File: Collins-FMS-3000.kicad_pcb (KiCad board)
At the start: 2 copper layers, 145 x 160 mm, 138 parts, among them J1 USB_B_Mini, J2 AVR-ISP-6, J3 Conn_01x04, SW1 SW_Push_LED, SW10 SW_Push_LED, SW11 SW_Push_LED, SW12 SW_Push_LED, SW13 SW_Push_LED, SW14 SW_Push_LED, SW15 SW_Push_LED, SW16 SW_Push_LED, SW17 SW_Push_LED, SW18 SW_Push_LED, SW19 SW_Push_LED, SW2 SW_Push_LED, SW20 SW_Push_LED, SW21 SW_Push_LED, SW22 SW_Push_LED, SW23 SW_Push_LED, SW24 SW_Push_LED, SW25 SW_Push_LED, SW26 SW_Push_LED, SW27 SW_Push_LED, SW28 SW_Push_LED, SW29 SW_Push_LED, SW3 SW_Push_LED, SW30 SW_Push_LED, SW31 SW_Push_LED, SW32 SW_Push_LED, SW33 SW_Push_LED, SW34 SW_Push_LED, SW35 SW_Push_LED, SW36 SW_Push_LED, SW37 SW_Push_LED, SW38 SW_Push_LED, SW39 SW_Push_LED, SW4 SW_Push_LED, SW40 SW_Push_LED, SW41 SW_Push_LED, SW42 SW_Push_LED, SW43 SW_Push_LED, SW44 SW_Push_LED, SW45 SW_Push_LED, SW46 SW_Push_LED, SW47 SW_Push_LED, SW48 SW_Push_LED, SW49 SW_Push_LED, SW5 SW_Push_LED, SW50 SW_Push_LED, SW51 SW_Push_LED, SW52 SW_Push_LED, SW53 SW_Push_LED, SW54 SW_Push_LED, SW55 SW_Push_LED, SW56 SW_Push_LED, SW57 SW_Push_LED, SW58 SW_Push_LED, SW59 SW_Push_LED, SW6 SW_Push_LED, SW60 SW_Push_LED, SW61 SW_Push_LED, SW62 SW_Push_LED, SW63 SW_Push_LED, SW64 SW_Push_LED, SW65 SW_Push_LED, SW66 SW_Push_LED, SW67 SW_Push_LED, SW68 SW_Push_LED, SW69 SW_Push_LED, SW7 SW_Push_LED, SW70 SW_Push, SW8 SW_Push_LED, SW9 SW_Push_LED, U1 ATmega32U4-MU, U2 MCP23017_SO, U3 MCP23017_SO, U4 IS31FL3733B, Y1 16MHz

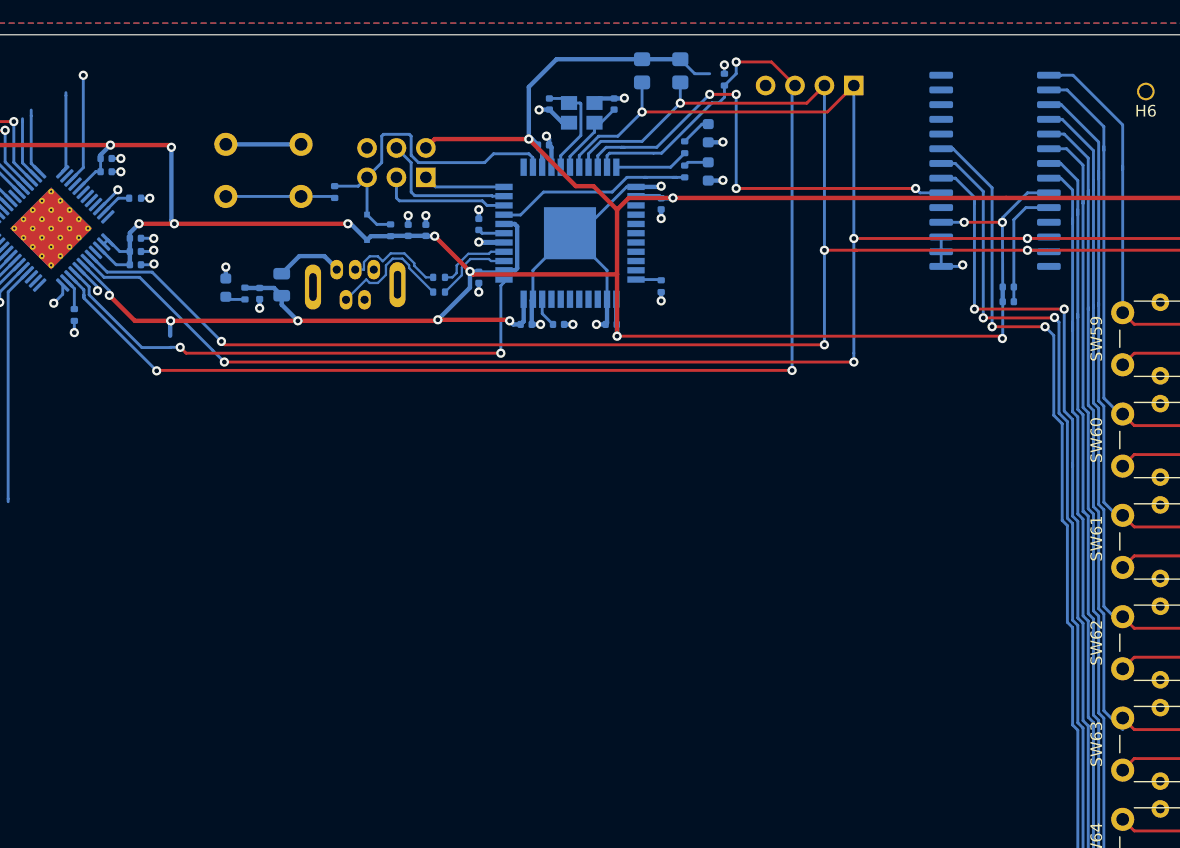
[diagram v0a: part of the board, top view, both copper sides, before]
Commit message: Add ROW INTB, new debug header
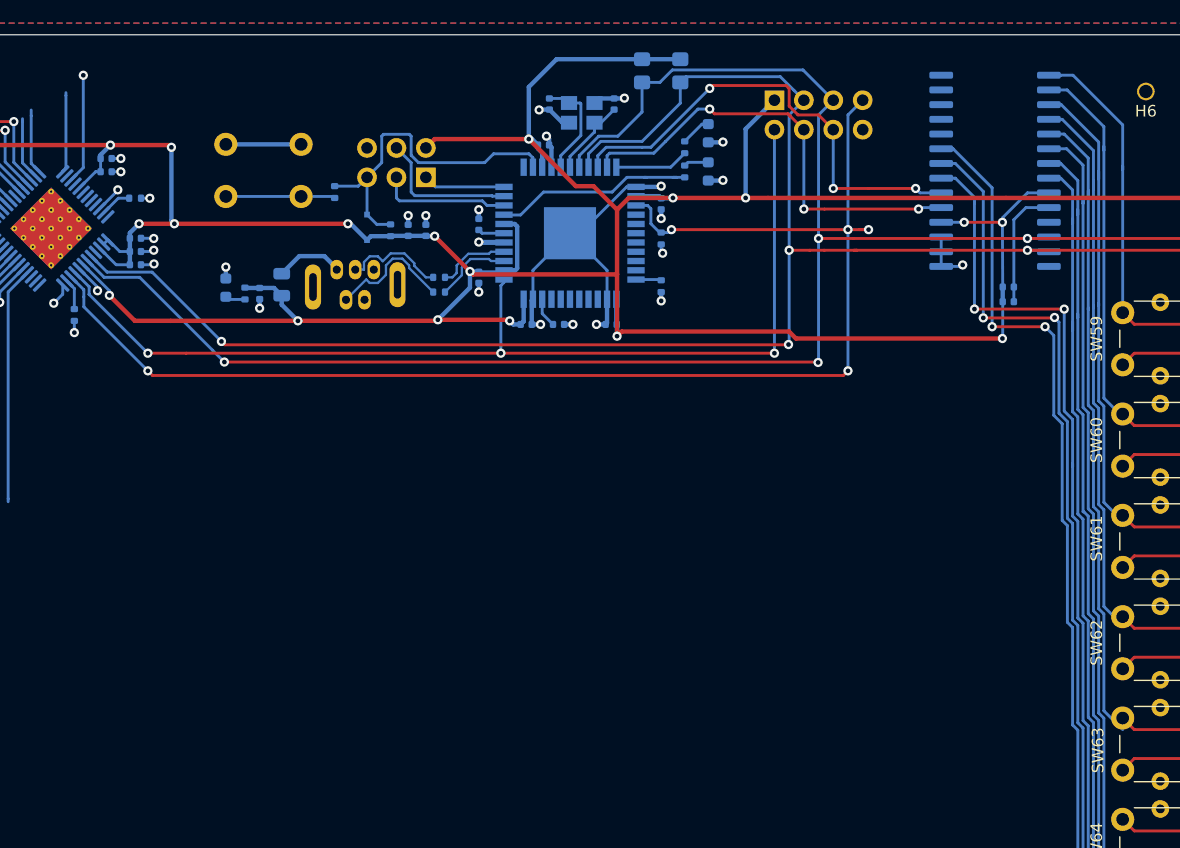
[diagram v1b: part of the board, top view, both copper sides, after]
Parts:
- J3: value Conn_01x04 -> Conn_02x04_Odd_Even; footprint Connector_PinHeader_2.54mm:PinHeader_1x04_P2.54mm_Vertical -> Connector_PinHeader_2.54mm:PinHeader_2x04_P2.54mm_Vertical
- moved R3 14.8 mm to (112.6, 37.6), turned to 270 degrees
- moved J3 6.97 mm to (122.4, 25.7), turned to 270 degrees
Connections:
- J3 pad 1: I2C_SCL -> +5V
- J3 pad 2: I2C_SDA -> LED_INTB
- J3 pad 3: SDB -> I2C_SDA
- J3 pad 4: GND -> ROW_INTB
- U1 pad 21: SDB -> ROW_INTB
- U1 pad 25: Net-(U1-Pad25) -> SDB
- U2 pad 19: Net-(U2-Pad19) -> ROW_INTB
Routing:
- net LED_INTB: track 46.5 -> 89.4 mm, vias 2 -> 3
- net ROW_INTB: track 0.00 -> 39.3 mm, vias 0 -> 3
- net +5V: track 485.8 -> 491.5 mm
- net SDB: track 113.5 -> 117.6 mm, vias 3 -> 5
- net I2C_SDA: track 299.6 -> 297.5 mm, vias 8 -> 7
- net I2C_SCL: track 305.6 -> 303.7 mm, vias 8 -> 7
- net ROW_INTA: track 41.4 -> 40.9 mm, vias 4 -> 3
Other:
- board text added: "LINTB"
- board text added: "RINTA"
- board text added: "RINTB"

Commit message: Change ISET to 47k Fixes #3
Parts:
- R6: value 20k -> 47k

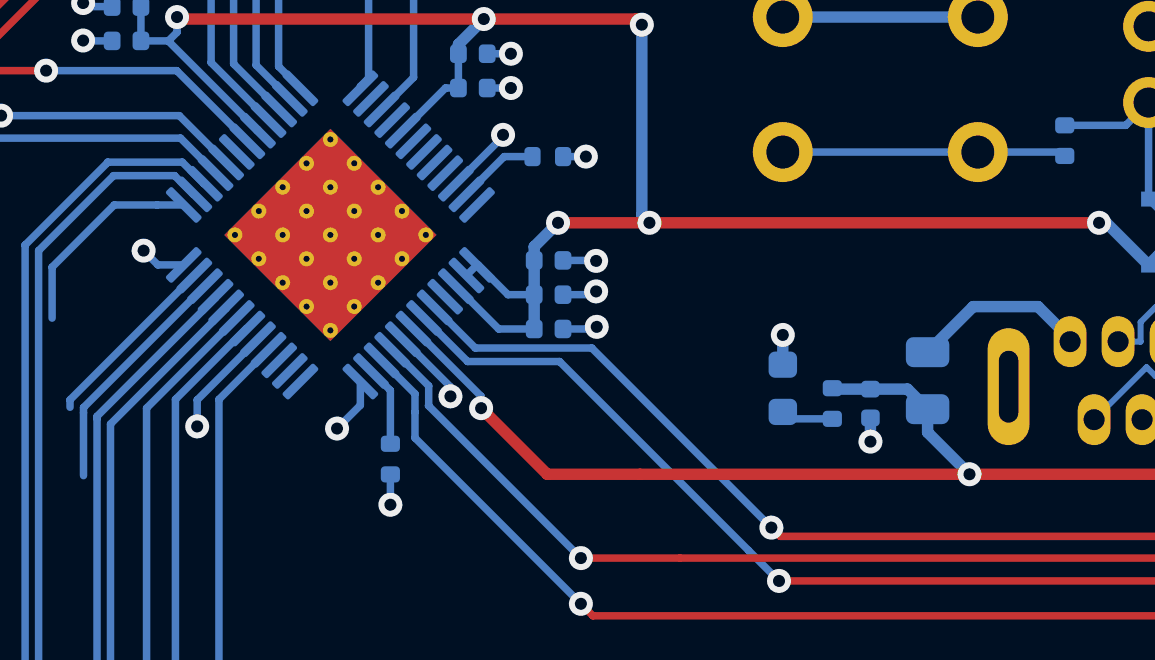
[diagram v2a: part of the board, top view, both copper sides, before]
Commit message: Connect thermal pad to ground pins (#5)
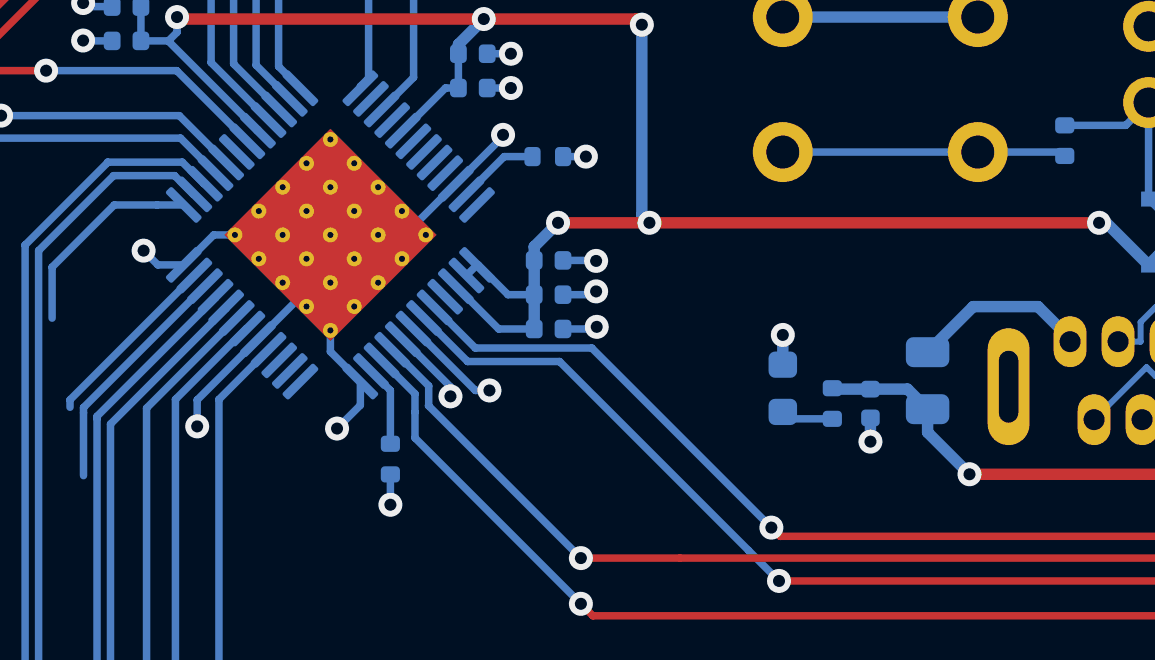
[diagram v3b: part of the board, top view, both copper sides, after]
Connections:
- U4 pad 49: (no net) -> GND
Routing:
- net +5V: track 491.5 -> 467.7 mm, vias 20 -> 19
- net GND: track 108.4 -> 131.7 mm, vias 35 -> 36

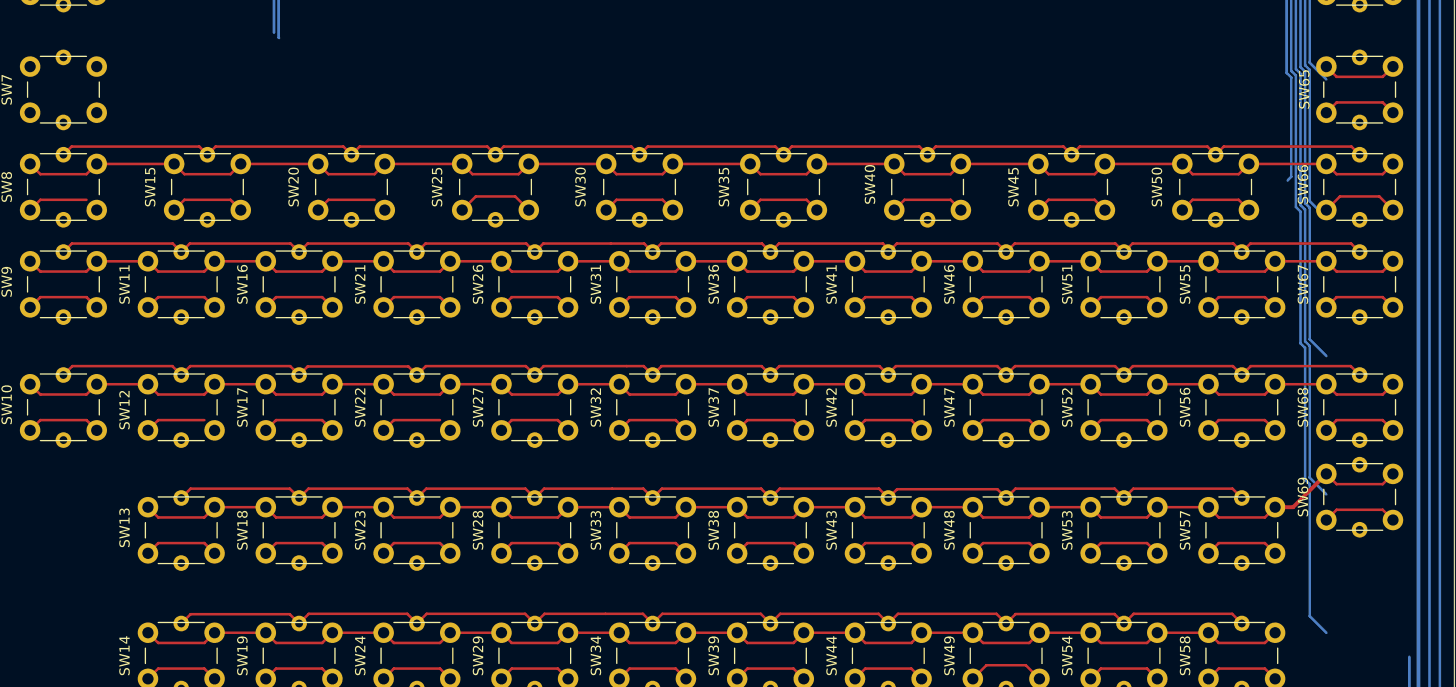
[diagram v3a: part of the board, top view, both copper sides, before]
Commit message: Fix pad clearence DRC errors
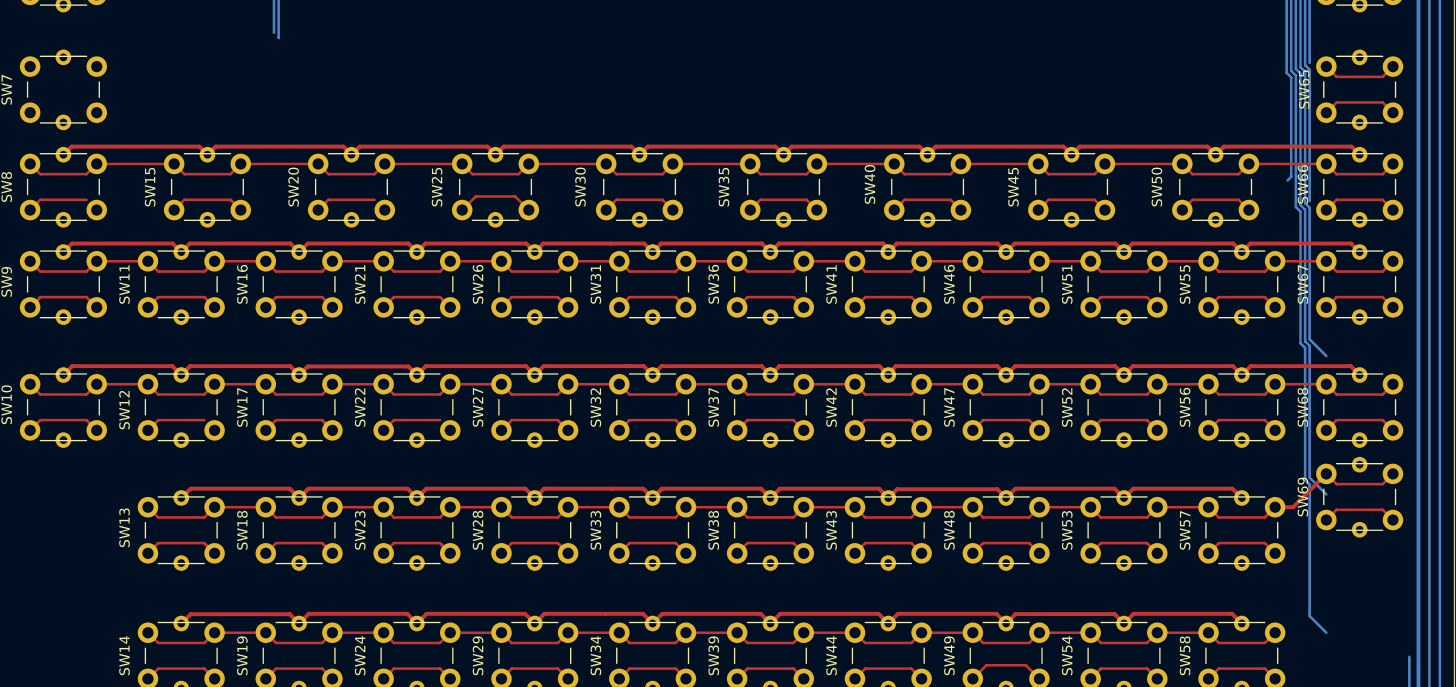
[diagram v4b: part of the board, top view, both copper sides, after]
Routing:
- net Net-(D66-Pad2): track 7.60 -> 0.00 mm
- net /ButtonMatrix/COL11: track 97.5 -> 104.8 mm
- net /ButtonMatrix/ROW6: track 94.7 -> 92.4 mm
- net /ButtonMatrix/ROW5: track 89.2 -> 86.9 mm
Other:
- net class SW traces added: clearance 0.2, trace_width 0.381, via_dia 0.8, via_drill 0.4
- rule via_min_size: 0.4 -> 0.6

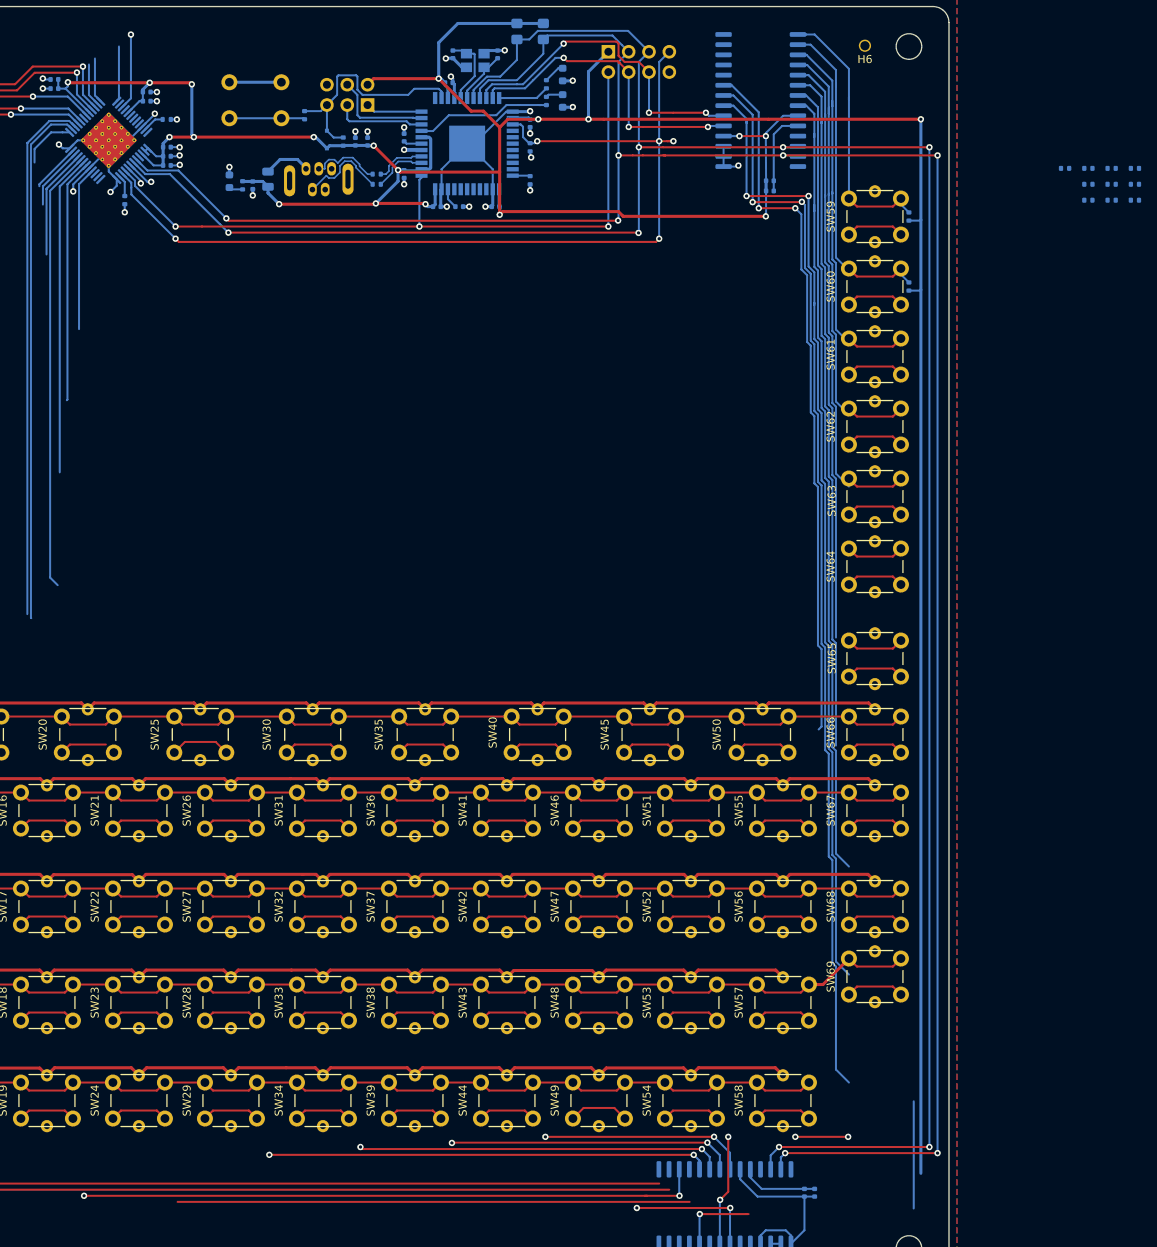
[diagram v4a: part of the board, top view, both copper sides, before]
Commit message: Use perfect 0402 pad dimensions
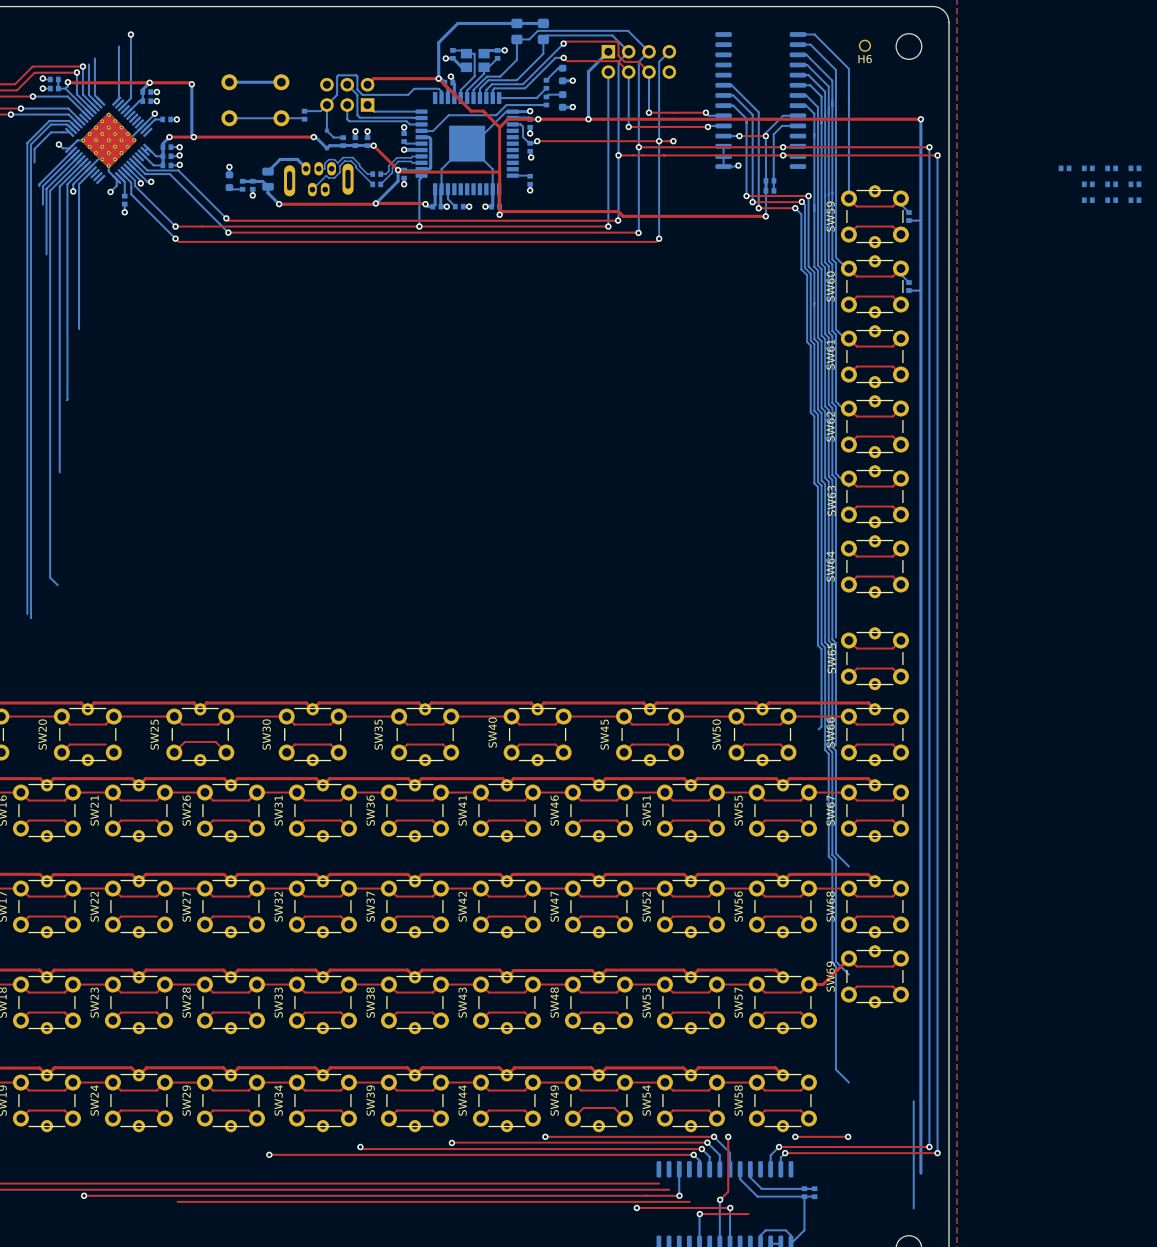
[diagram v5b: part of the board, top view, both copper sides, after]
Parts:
- C1, C10, C11, C12, C13, C14, C15, C16, C17, C18, C19, C2, C20, C22, C23, C24, C25, C26, C27, C28, C3, C4, C9: footprint Capacitor_SMD:C_0402_1005Metric -> Collins-FMS-3000:Perfect_0402
- R10, R11, R12, R13, R14, R15, R16, R17, R18, R19, R21, R22, R23, R24, R25, R26, R27, R28, R3, R6, R7, R8, R9: footprint Resistor_SMD:R_0402_1005Metric -> Collins-FMS-3000:Perfect_0402

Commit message: New PCB size and hole placement
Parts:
- added H10: MountingHole, MountingHole:MountingHole_3.2mm_M3, F.Cu at (388.9, 229.7)
- added H11: MountingHole, MountingHole:MountingHole_3.2mm_M3, F.Cu at (359.3, 248.9)
- added H12: MountingHole, MountingHole:MountingHole_3.2mm_M3, F.Cu at (470.5, 229.7)
- added H13: MountingHole, MountingHole:MountingHole_3.2mm_M3, F.Cu at (497.4, 248.9)
- added H14: MountingHole, MountingHole:MountingHole_3.2mm_M3, F.Cu at (388.9, 244.0)
- added H15: MountingHole, MountingHole:MountingHole_3.2mm_M3, F.Cu at (454.0, 244.0)
- added H8: MountingHole, MountingHole:MountingHole_3.2mm_M3, F.Cu at (388.9, 191.3)
- added H9: MountingHole, MountingHole:MountingHole_3.2mm_M3, F.Cu at (470.5, 191.3)
- moved H2 451.4 mm to (497.5, 324.8)
- moved H1 449.2 mm to (359.5, 324.8)
- moved H4 337.7 mm to (497.7, 170.7)
- moved H3 334.6 mm to (359.6, 170.7)
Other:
- board size 145 x 160 mm -> 481.1 x 309.2 mm

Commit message: All buttons placed
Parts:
- removed H5, H6, H7: MountingHole, Collins-FMS-3000:JLCPCB_Tooling_Hole
- removed R10, R11, R12, R13, R14, R15, R16, R17, R18, R19, R8, R9: 2k2, Collins-FMS-3000:Perfect_0402
- moved SW58 377.9 mm to (480.6, 320.3)
- moved SW57 377.4 mm to (480.6, 306.8)
- moved SW54 377.3 mm to (468.4, 320.3)
- moved SW53 376.7 mm to (468.4, 306.8)
- moved SW56 376.7 mm to (480.6, 293.4)
- moved SW49 376.6 mm to (456.2, 320.3)
- moved SW48 376.1 mm to (456.2, 306.8)
- moved SW52 376.1 mm to (468.4, 293.4)
- moved SW55 376.1 mm to (480.6, 279.9)
- moved SW44 376.0 mm to (444.0, 320.3)
- moved SW67 375.7 mm to (492.3, 278.6)
- moved SW43 375.5 mm to (444.0, 306.8)
- moved SW47 375.5 mm to (456.2, 293.4)
- moved SW51 375.5 mm to (468.4, 279.9)
- moved SW39 375.4 mm to (431.8, 320.3)
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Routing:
- net /ButtonMatrix/ROW9: track 287.8 -> 91.5 mm
- net /ButtonMatrix/ROW8: track 264.8 -> 92.6 mm
- net /ButtonMatrix/COL0: track 164.6 -> 0.30 mm
- net /ButtonMatrix/ROW7: track 240.8 -> 83.8 mm
- net /LEDMatrix/SW10: track 141.4 -> 6.95 mm
- net /LEDMatrix/SW9: track 140.4 -> 6.11 mm
- net /ButtonMatrix/ROW10: track 221.0 -> 88.5 mm
- net /LEDMatrix/SW8: track 140.4 -> 7.99 mm
- net /ButtonMatrix/COL2: track 118.6 -> 0.00 mm, vias 2 -> 0
- net /ButtonMatrix/ROW11: track 118.3 -> 0.00 mm
- net /ButtonMatrix/COL1: track 113.8 -> 0.00 mm
- net /LEDMatrix/SW12: track 177.0 -> 66.3 mm
- net /LEDMatrix/SW11: track 176.3 -> 65.7 mm
- net /ButtonMatrix/COL11: track 104.8 -> 0.00 mm, vias 1 -> 0
- net /ButtonMatrix/COL3: track 100.2 -> 0.00 mm
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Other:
- board size 481.1 x 309.2 mm -> 145 x 161 mm
